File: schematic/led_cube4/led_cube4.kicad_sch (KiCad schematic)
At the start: 0 parts

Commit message: feat(schematic): add power module
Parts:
- added C1: 470u, symbol Device:C_Polarized
- added C2: 470n, symbol Device:C
- added C3: 100n, symbol Device:C
- added C4: 10u, symbol Device:C_Polarized
- added J1: (no value), symbol Connector:Screw_Terminal_01x02
- added U1: L7805, symbol Regulator_Linear:L7805
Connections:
- new net: C1.1, C2.1, J1.1 (Pin_1), U1.1 (IN)
- new net +5V: C3.1, C4.1, U1.3 (OUT)
- new net GND: C1.2, C2.2, C3.2, C4.2, J1.2 (Pin_2), U1.2 (GND)

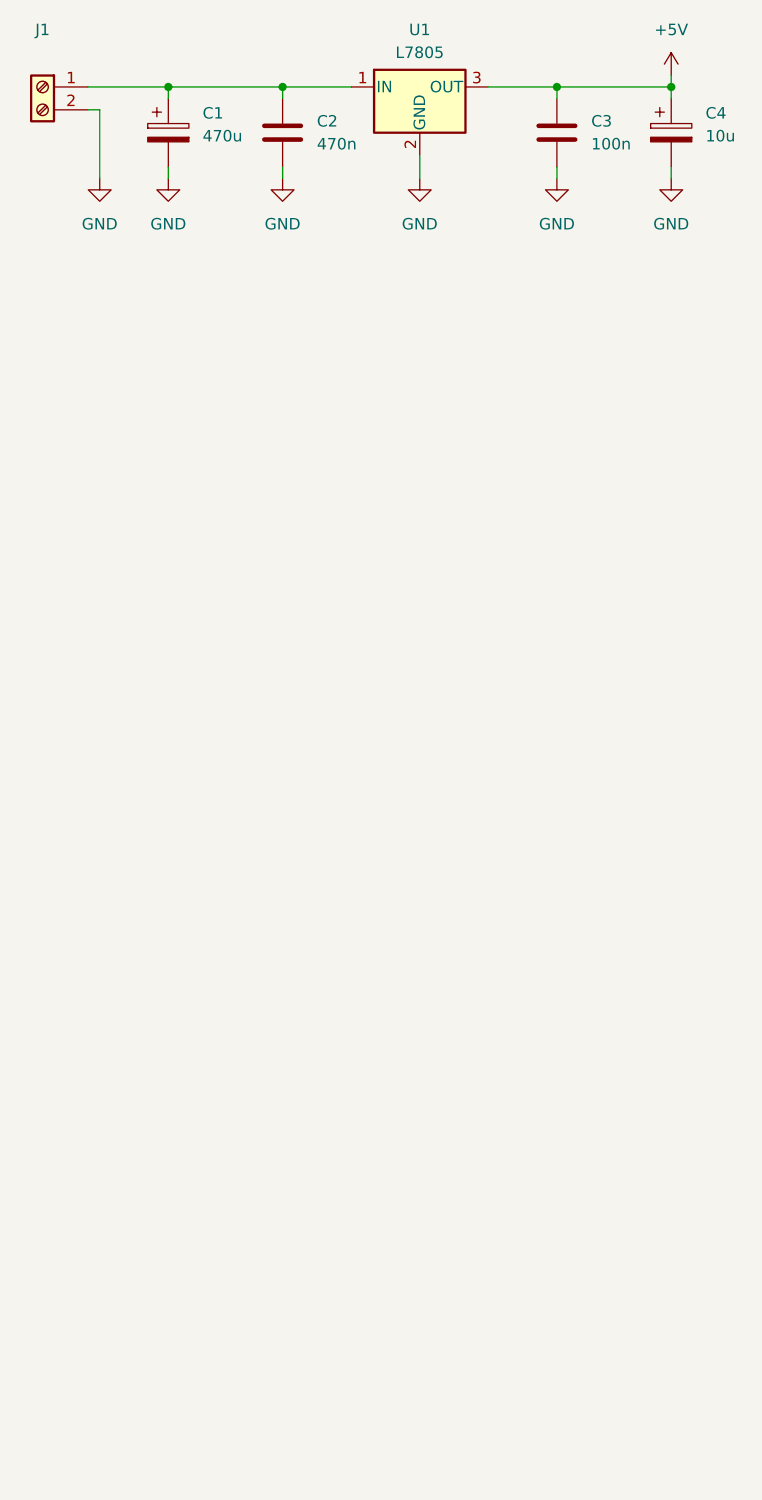
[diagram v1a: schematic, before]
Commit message: feat(schematic): add microcontroller
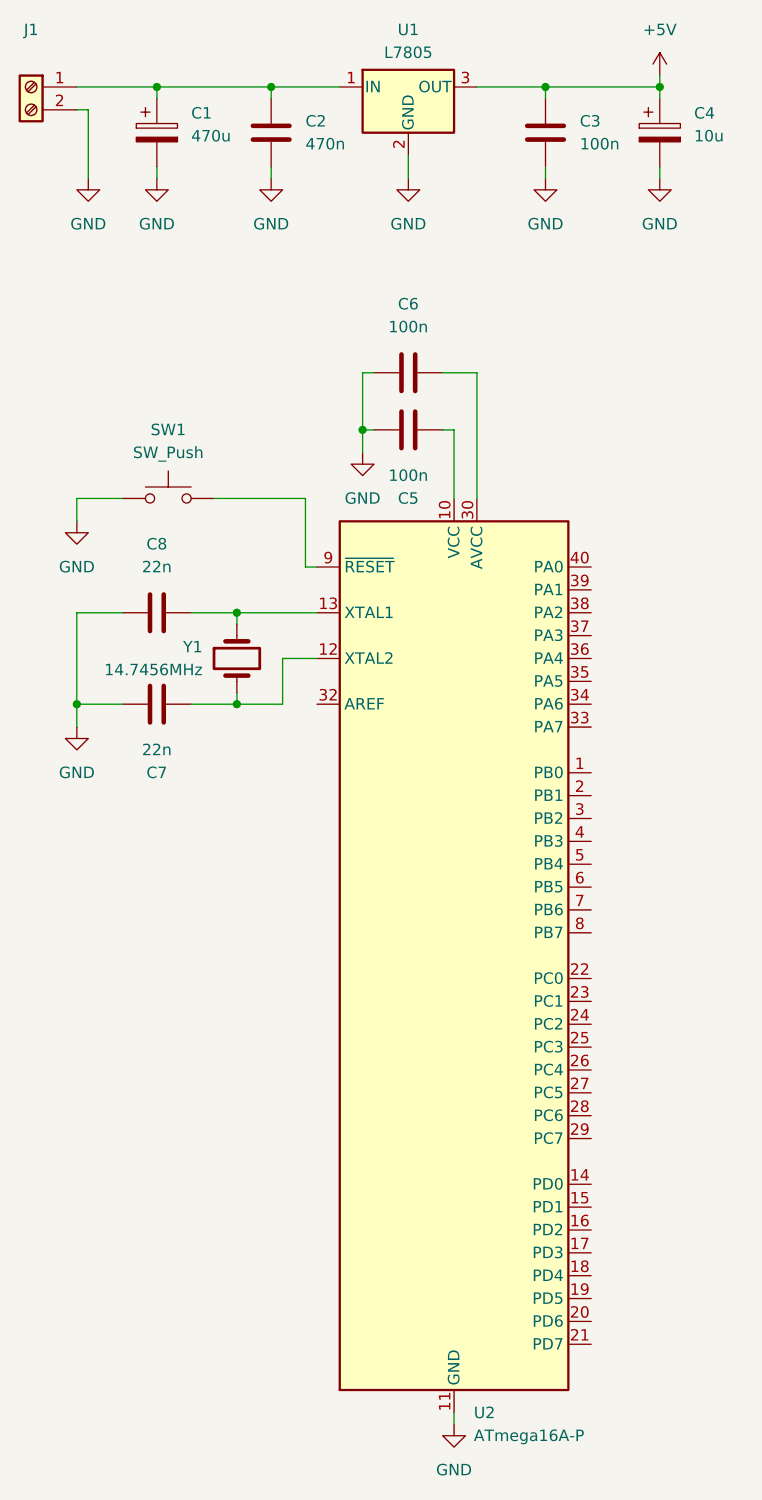
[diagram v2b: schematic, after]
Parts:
- added C5, C6: 100n, symbol Device:C
- added C7, C8: 22n, symbol Device:C
- added SW1: SW_Push, symbol Switch:SW_Push
- added U2: ATmega16A-P, Package_DIP:DIP-40_W15.24mm, symbol MCU_Microchip_ATmega:ATmega16A-P
- added Y1: 14.7456MHz, Crystal:Crystal_AT310_D3.0mm_L10.0mm_Horizontal, symbol Device:Crystal
- J1: value (none) -> ~
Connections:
- net GND: now also C5.1, C6.1, C7.1, C8.1, SW1.1, U2.11 (GND), U2.31 (GND)
- new net: C6.2, U2.30 (AVCC)
- new net: C5.2, U2.10 (VCC)
- new net: C8.2, U2.13 (XTAL1), Y1.1
- new net: C7.2, U2.12 (XTAL2), Y1.2
- new net: SW1.2, U2.9 (~{RESET})
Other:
- moved on the sheet: C1, C2, C3, C4, J1, U1

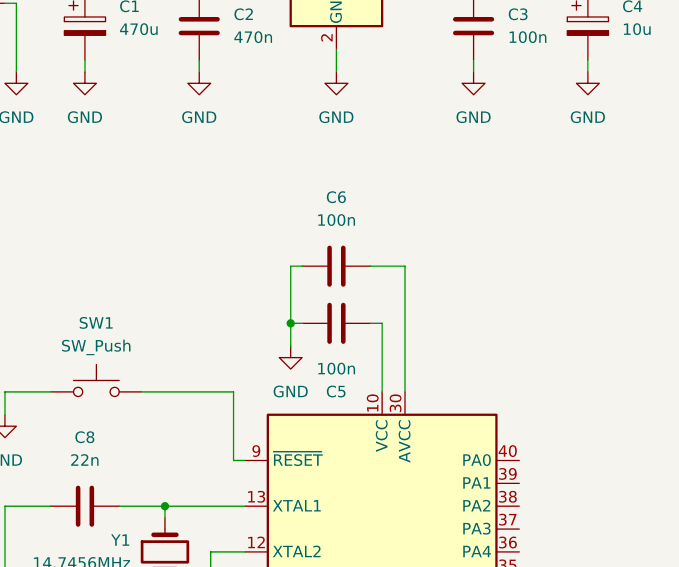
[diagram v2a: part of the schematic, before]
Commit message: fix(schematic): add +5V net label to VCC and AVCC uC pins
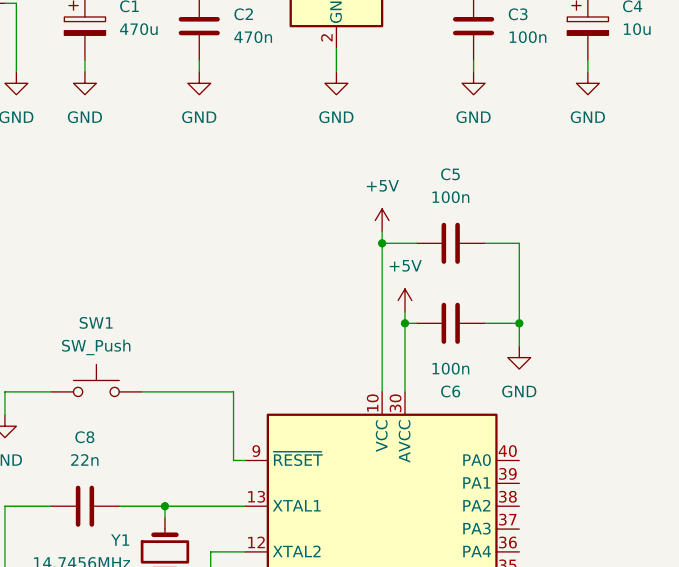
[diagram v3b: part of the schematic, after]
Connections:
- net +5V: now also C5.1, C6.1, U2.10 (VCC), U2.30 (AVCC)
- net GND: now also C5.2, C6.2; no longer C5.1, C6.1
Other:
- moved on the sheet: C5, C6
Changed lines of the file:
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@@
 (kicad_sch (version 20230121) (generator eeschema)
   (paper "A4")
+  (junction (at 92.71 68.58) (diameter 0) (color 0 0 0 0)
+  )
   (junction (at 57.15 30.48) (diameter 0) (color 0 0 0 0)
   )
+  (junction (at 77.47 59.69) (diameter 0) (color 0 0 0 0)
+  )
   (junction (at 44.45 30.48) (diameter 0) (color 0 0 0 0)
   )
@@
   (junction (at 35.56 99.06) (diameter 0) (color 0 0 0 0)
   )
-  (junction (at 67.31 68.58) (diameter 0) (color 0 0 0 0)
+  (junction (at 80.01 68.58) (diameter 0) (color 0 0 0 0)
   )
   (junction (at 53.34 88.9) (diameter 0) (color 0 0 0 0)
@@
   (junction (at 100.33 30.48) (diameter 0) (color 0 0 0 0)
   )
+  (wire (pts (xy 77.47 59.69) (xy 81.28 59.69))
+    (stroke (width 0) (type default))
+  )
   (wire (pts (xy 48.26 88.9) (xy 53.34 88.9))
     (stroke (width 0) (type default))
@@
     (stroke (width 0) (type default))
   )
-  (wire (pts (xy 67.31 62.23) (xy 67.31 68.58))
-    (stroke (width 0) (type default))
-  )
   (wire (pts (xy 44.45 39.37) (xy 44.45 40.64))
     (stroke (width 0) (type default))
@@
     (stroke (width 0) (type default))
   )
-  (wire (pts (xy 80.01 62.23) (xy 76.2 62.23))
+  (wire (pts (xy 80.01 68.58) (xy 81.28 68.58))
+    (stroke (width 0) (type default))
+  )
+  (wire (pts (xy 80.01 67.31) (xy 80.01 68.58))
     (stroke (width 0) (type default))
   )
@@
     (stroke (width 0) (type default))
   )
-  (wire (pts (xy 76.2 68.58) (xy 77.47 68.58))
-    (stroke (width 0) (type default))
-  )
   (wire (pts (xy 53.34 88.9) (xy 53.34 90.17))
     (stroke (width 0) (type default))
@@
     (stroke (width 0) (type default))
   )
+  (wire (pts (xy 88.9 59.69) (xy 92.71 59.69))
+    (stroke (width 0) (type default))
+  )
   (wire (pts (xy 87.63 30.48) (xy 87.63 31.75))
     (stroke (width 0) (type default))
@@
     (stroke (width 0) (type default))
   )
-  (wire (pts (xy 80.01 76.2) (xy 80.01 62.23))
+  (wire (pts (xy 80.01 76.2) (xy 80.01 68.58))
     (stroke (width 0) (type default))
   )
@@
     (stroke (width 0) (type default))
   )
-  (wire (pts (xy 68.58 68.58) (xy 67.31 68.58))
+  (wire (pts (xy 88.9 68.58) (xy 92.71 68.58))
     (stroke (width 0) (type default))
   )
@@
     (stroke (width 0) (type default))
   )
-  (wire (pts (xy 77.47 68.58) (xy 77.47 76.2))
+  (wire (pts (xy 92.71 68.58) (xy 92.71 71.12))
+    (stroke (width 0) (type default))
+  )
+  (wire (pts (xy 77.47 58.42) (xy 77.47 59.69))
     (stroke (width 0) (type default))
   )
@@
     (stroke (width 0) (type default))
   )
+  (wire (pts (xy 77.47 59.69) (xy 77.47 76.2))
+    (stroke (width 0) (type default))
+  )
   (wire (pts (xy 58.42 93.98) (xy 62.23 93.98))
     (stroke (width 0) (type default))
@@
     (stroke (width 0) (type default))
   )
-  (wire (pts (xy 68.58 62.23) (xy 67.31 62.23))
-    (stroke (width 0) (type default))
-  )
   (wire (pts (xy 100.33 30.48) (xy 100.33 31.75))
     (stroke (width 0) (type default))
@@
     (stroke (width 0) (type default))
   )
+  (wire (pts (xy 92.71 59.69) (xy 92.71 68.58))
+    (stroke (width 0) (type default))
+  )
   (wire (pts (xy 53.34 97.79) (xy 53.34 99.06))
     (stroke (width 0) (type default))
@@
     (stroke (width 0) (type default))
   )
-  (wire (pts (xy 67.31 68.58) (xy 67.31 71.12))
-    (stroke (width 0) (type default))
-  )
   (wire (pts (xy 36.83 33.02) (xy 35.56 33.02))
     (stroke (width 0) (type default))
@@
     )
   )
-  (symbol (lib_id "Device:C") (at 72.39 62.23 90) (unit 1)
-    (in_bom yes) (on_board yes) (dnp no) (fields_autoplaced)
-    (property "Reference" "C6" (at 72.39 54.61 90)
-      (effects (font (size 1.27 1.27)))
-    )
-    (property "Value" "100n" (at 72.39 57.15 90)
-      (effects (font (size 1.27 1.27)))
-    )
-    (property "Footprint" "" (at 76.2 61.2648 0)
-      (effects (font (size 1.27 1.27)) hide)
-    )
-    (property "Datasheet" "~" (at 72.39 62.23 0)
+  (symbol (lib_id "Device:C") (at 85.09 68.58 90) (mirror x) (unit 1)
+    (in_bom yes) (on_board yes) (dnp no)
+    (property "Reference" "C6" (at 85.09 76.2 90)
+      (effects (font (size 1.27 1.27)))
+    )
+    (property "Value" "100n" (at 85.09 73.66 90)
+      (effects (font (size 1.27 1.27)))
+    )
+    (property "Footprint" "" (at 88.9 69.5452 0)
+      (effects (font (size 1.27 1.27)) hide)
+    )
+    (property "Datasheet" "~" (at 85.09 68.58 0)
       (effects (font (size 1.27 1.27)) hide)
     )
@@
     )
   )
-  (symbol (lib_id "Device:C") (at 72.39 68.58 90) (mirror x) (unit 1)
+  (symbol (lib_id "Device:C") (at 85.09 59.69 90) (unit 1)
     (in_bom yes) (on_board yes) (dnp no)
-    (property "Reference" "C5" (at 72.39 76.2 90)
-      (effects (font (size 1.27 1.27)))
-    )
-    (property "Value" "100n" (at 72.39 73.66 90)
-      (effects (font (size 1.27 1.27)))
-    )
-    (property "Footprint" "" (at 76.2 69.5452 0)
-      (effects (font (size 1.27 1.27)) hide)
-    )
-    (property "Datasheet" "~" (at 72.39 68.58 0)
+    (property "Reference" "C5" (at 85.09 52.07 90)
+      (effects (font (size 1.27 1.27)))
+    )
+    (property "Value" "100n" (at 85.09 54.61 90)
+      (effects (font (size 1.27 1.27)))
+    )
+    (property "Footprint" "" (at 88.9 58.7248 0)
+      (effects (font (size 1.27 1.27)) hide)
+    )
+    (property "Datasheet" "~" (at 85.09 59.69 0)
       (effects (font (size 1.27 1.27)) hide)
     )
@@
     )
   )
+  (symbol (lib_id "power:+5V") (at 77.47 58.42 0) (unit 1)
+    (in_bom yes) (on_board yes) (dnp no) (fields_autoplaced)
+    (property "Reference" "#PWR012" (at 77.47 62.23 0)
+      (effects (font (size 1.27 1.27)) hide)
+    )
+    (property "Value" "+5V" (at 77.47 53.34 0)
+      (effects (font (size 1.27 1.27)))
+    )
+    (property "Footprint" "" (at 77.47 58.42 0)
+      (effects (font (size 1.27 1.27)) hide)
+    )
+    (property "Datasheet" "" (at 77.47 58.42 0)
+      (effects (font (size 1.27 1.27)) hide)
+    )
+    (pin "1")
+    (instances
+      (project "led_cube4"
+        (path "/44967cb4-81e9-43f0-83d3-71e4b89b9f9f"
+          (reference "#PWR012") (unit 1)
+        )
+      )
+    )
+  )
   (symbol (lib_id "power:GND") (at 36.83 40.64 0) (unit 1)
     (in_bom yes) (on_board yes) (dnp no) (fields_autoplaced)
@@
     )
   )
+  (symbol (lib_id "power:+5V") (at 80.01 67.31 0) (unit 1)
+    (in_bom yes) (on_board yes) (dnp no) (fields_autoplaced)
+    (property "Reference" "#PWR013" (at 80.01 71.12 0)
+      (effects (font (size 1.27 1.27)) hide)
+    )
+    (property "Value" "+5V" (at 80.01 62.23 0)
+      (effects (font (size 1.27 1.27)))
+    )
+    (property "Footprint" "" (at 80.01 67.31 0)
+      (effects (font (size 1.27 1.27)) hide)
+    )
+    (property "Datasheet" "" (at 80.01 67.31 0)
+      (effects (font (size 1.27 1.27)) hide)
+    )
+    (pin "1")
+    (instances
+      (project "led_cube4"
+        (path "/44967cb4-81e9-43f0-83d3-71e4b89b9f9f"
+          (reference "#PWR013") (unit 1)
+        )
+      )
+    )
+  )
   (symbol (lib_id "power:GND") (at 44.45 40.64 0) (unit 1)
     (in_bom yes) (on_board yes) (dnp no) (fields_autoplaced)
@@
     )
   )
-  (symbol (lib_id "power:GND") (at 67.31 71.12 0) (unit 1)
-    (in_bom yes) (on_board yes) (dnp no) (fields_autoplaced)
-    (property "Reference" "#PWR09" (at 67.31 77.47 0)
-      (effects (font (size 1.27 1.27)) hide)
-    )
-    (property "Value" "GND" (at 67.31 76.2 0)
-      (effects (font (size 1.27 1.27)))
-    )
-    (property "Footprint" "" (at 67.31 71.12 0)
-      (effects (font (size 1.27 1.27)) hide)
-    )
-    (property "Datasheet" "" (at 67.31 71.12 0)
-      (effects (font (size 1.27 1.27)) hide)
-    )
+  (symbol (lib_id "power:GND") (at 92.71 71.12 0) (unit 1)
+    (in_bom yes) (on_board yes) (dnp no) (fields_autoplaced)
+    (property "Reference" "#PWR09" (at 92.71 77.47 0)
+      (effects (font (size 1.27 1.27)) hide)
+    )
+    (property "Value" "GND" (at 92.71 76.2 0)
+      (effects (font (size 1.27 1.27)))
+    )
+    (property "Footprint" "" (at 92.71 71.12 0)
+      (effects (font (size 1.27 1.27)) hide)
+    )
+    (property "Datasheet" "" (at 92.71 71.12 0)
+      (effects (font (size 1.27 1.27)) hide)
+    )
